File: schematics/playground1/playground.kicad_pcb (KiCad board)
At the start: 2 copper layers, 92.5 x 68.5 mm, 65 parts, among them J1 Conn_01x05, J2 Conn_02x03_Odd_Even, J3 Conn_01x03, J4 Conn_02x04_Odd_Even, SW1 SW_SPST, SW2 SW_Push, SW3 SW_Push, U1 ADS1299, U2 MCP1700x-330xxTT, U3 PIC32MX250F128B_I_SS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

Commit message: fixed all errors for pcb with no audio or ble
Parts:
- moved H1 0.50 mm to (96.0, 70.0)
- moved H2 0.50 mm to (180.5, 70.0)
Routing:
- net /AVDD_5V: track 90.4 -> 149.4 mm, vias 5 -> 8
- net /MCLR: track 45.2 -> 88.2 mm, vias 2 -> 8
- net /DGND: track 28.5 -> 67.7 mm, vias 5 -> 7
- net /DVDD_3V3: track 199.4 -> 232.0 mm, vias 4 -> 7
- net /RXD: track 46.9 -> 44.4 mm
- net /1P: track 20.4 -> 21.2 mm, vias 3 -> 2
- net /AGND: track 45.0 -> 45.3 mm, vias 13 -> 14
- net /BOOT_EN: vias 2 -> 4
- net /MOSI: vias 3 -> 2

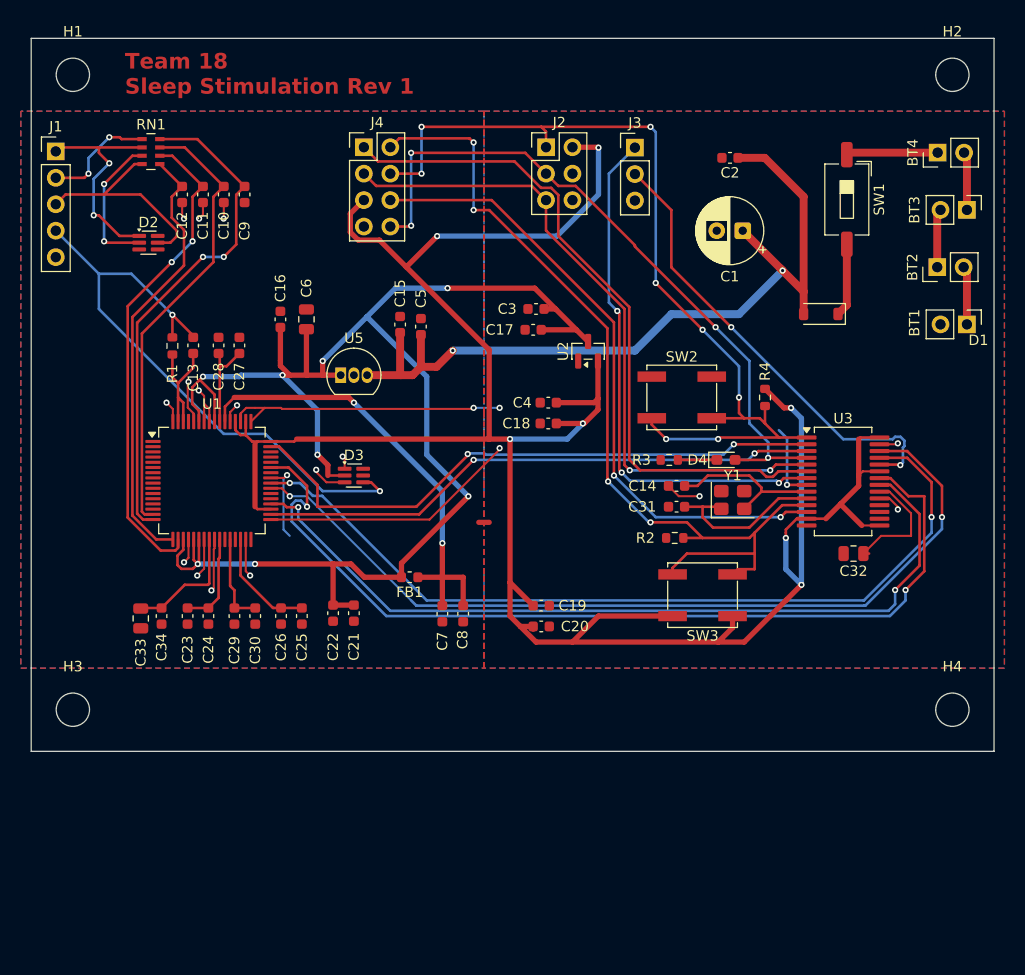
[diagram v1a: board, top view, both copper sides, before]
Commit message: add bluetooth chip to schematic and pcb
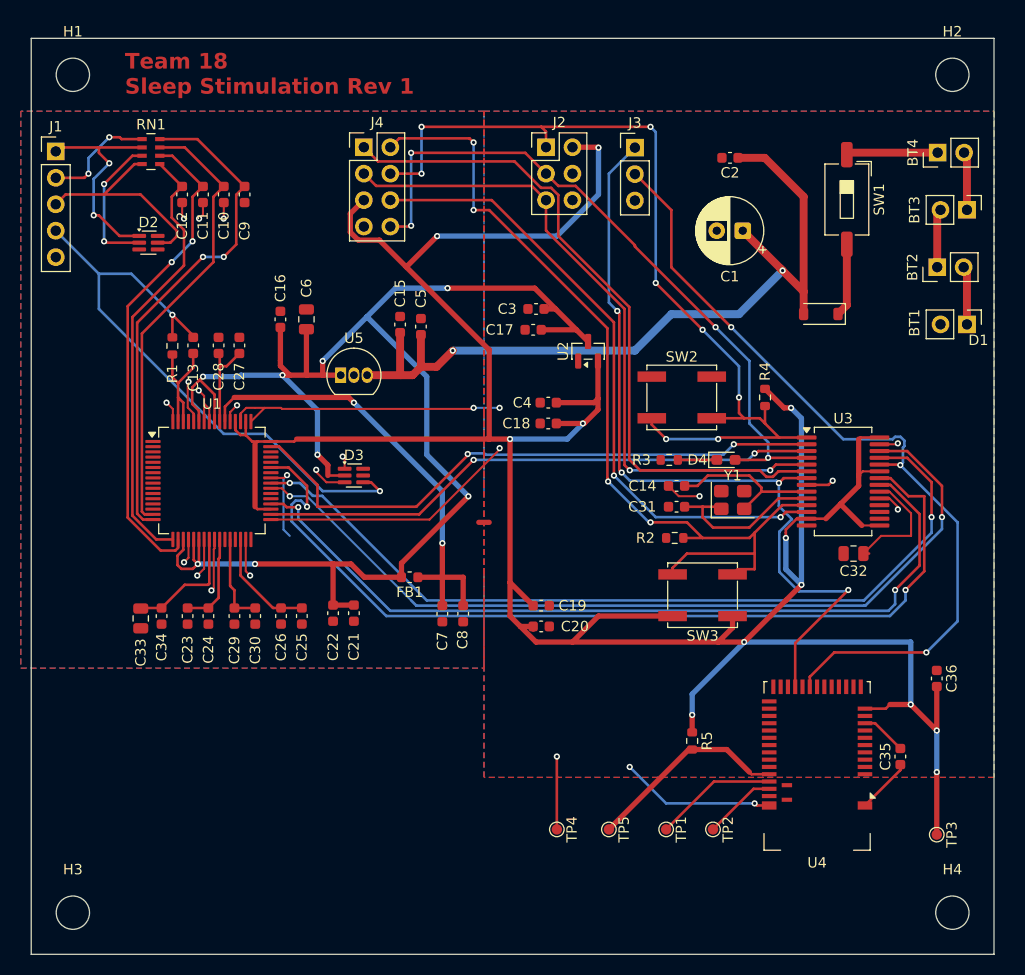
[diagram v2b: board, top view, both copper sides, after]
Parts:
- added C35: 1 µF, Capacitor_SMD:C_0603_1608Metric, F.Cu at (175.5, 135.5)
- added C36: 0.1 µF, Capacitor_SMD:C_0603_1608Metric, F.Cu at (179.0, 128.0)
- added R5: 10k, Resistor_SMD:R_0603_1608Metric, F.Cu at (155.5, 134.0)
- added TP1: TestPoint, TestPoint:TestPoint_Pad_D1.0mm, F.Cu at (153.0, 142.5)
- added TP2: TestPoint, TestPoint:TestPoint_Pad_D1.0mm, F.Cu at (157.5, 142.5)
- added TP3: TestPoint, TestPoint:TestPoint_Pad_D1.0mm, F.Cu at (179.0, 143.0)
- added TP4: TestPoint, TestPoint:TestPoint_Pad_D1.0mm, F.Cu at (142.5, 142.5)
- added TP5: TestPoint, TestPoint:TestPoint_Pad_D1.0mm, F.Cu at (147.5, 142.5)
- added U4: MDBT42Q-512K, ble_footprints:Raytac_MDBT42Q, F.Cu at (167.5, 136.4)
- moved H3 19.5 mm to (96.0, 150.5)
- moved H4 19.5 mm to (180.5, 150.5)
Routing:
- net /DVDD_3V3: track 232.0 -> 287.0 mm, vias 7 -> 12
- net /RXD: track 44.4 -> 79.1 mm, vias 2 -> 3
- net /TXD: track 51.1 -> 79.6 mm, vias 3 -> 4
- net /DGND: track 67.7 -> 90.2 mm, vias 7 -> 10
- net Net-(U4-P0.21/~{RESET}): track 0.00 -> 19.6 mm
- net Net-(U4-SWDCLK): track 0.00 -> 11.8 mm
- net Net-(U4-SWDIO): track 0.00 -> 7.02 mm
- net Net-(U4-DEC4): track 0.00 -> 4.40 mm
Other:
- board size 92.5 x 68.5 mm -> 92.5 x 88 mm

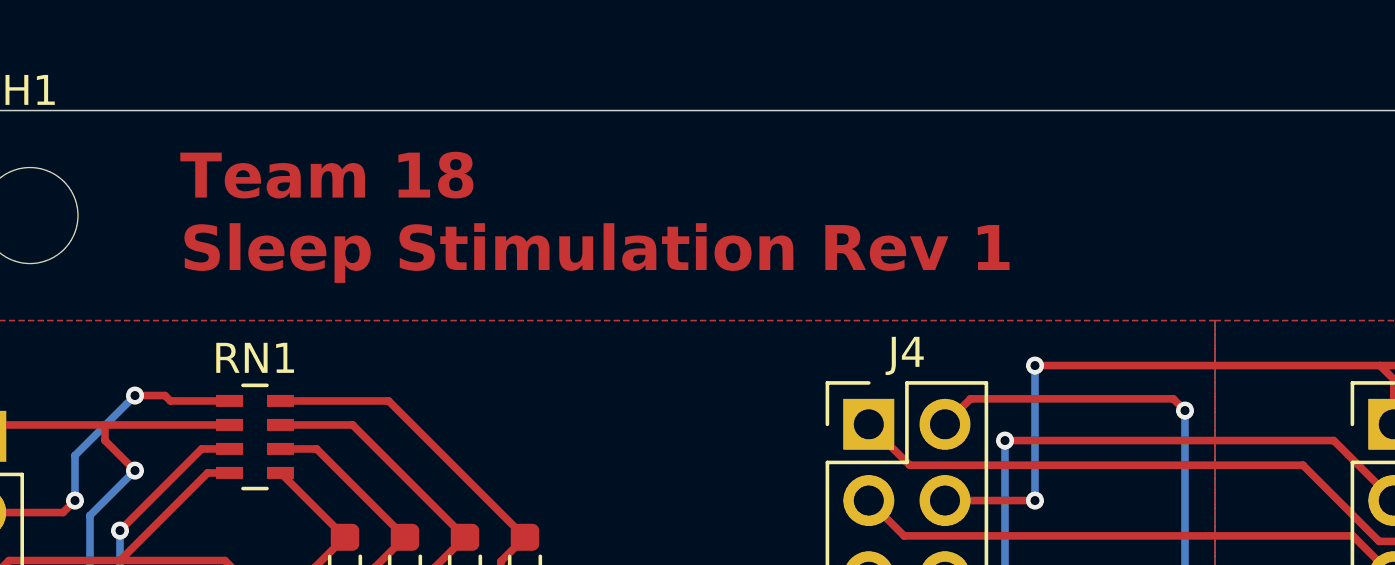
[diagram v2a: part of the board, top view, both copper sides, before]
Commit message: updated revision number for pcb
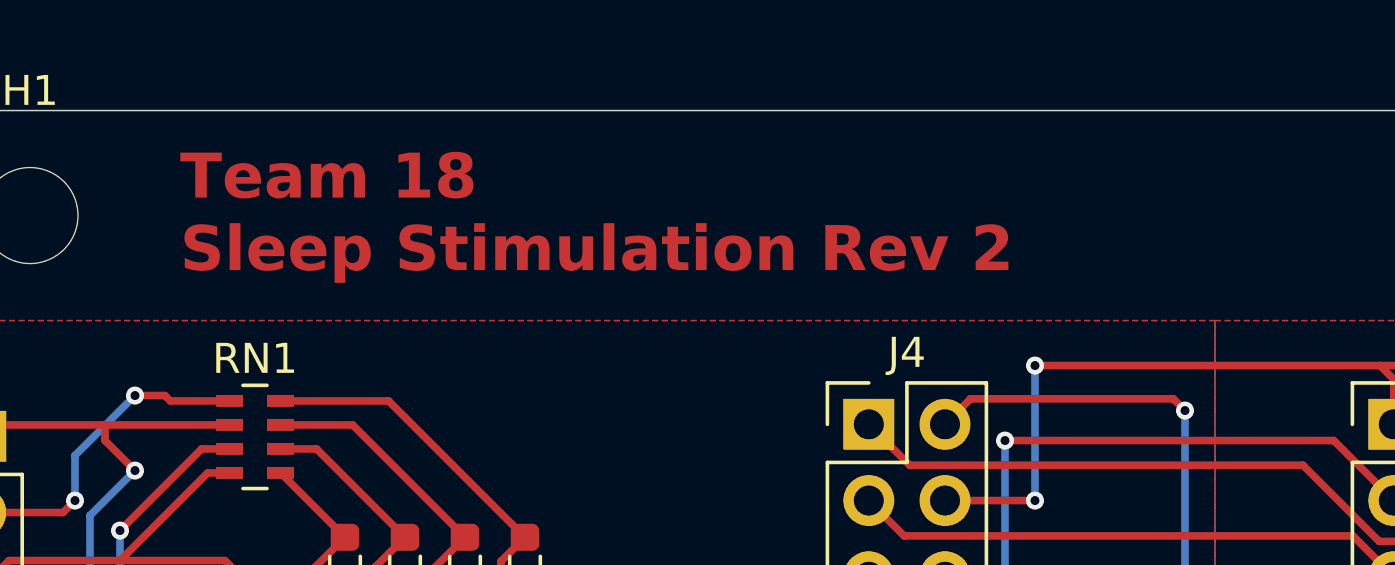
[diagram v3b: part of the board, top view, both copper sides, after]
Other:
- board text added: "Team 18 Sleep Stimulation Rev 2"
- board text removed: "Team 18 Sleep Stimulation Rev 1"
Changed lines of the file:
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@@
 		(layer "Edge.Cuts")
 	)
-	(gr_text "Team 18\nSleep Stimulation Rev 1"
+	(gr_text "Team 18\nSleep Stimulation Rev 2"
 		(at 101 72 0)
 		(layer "F.Cu")

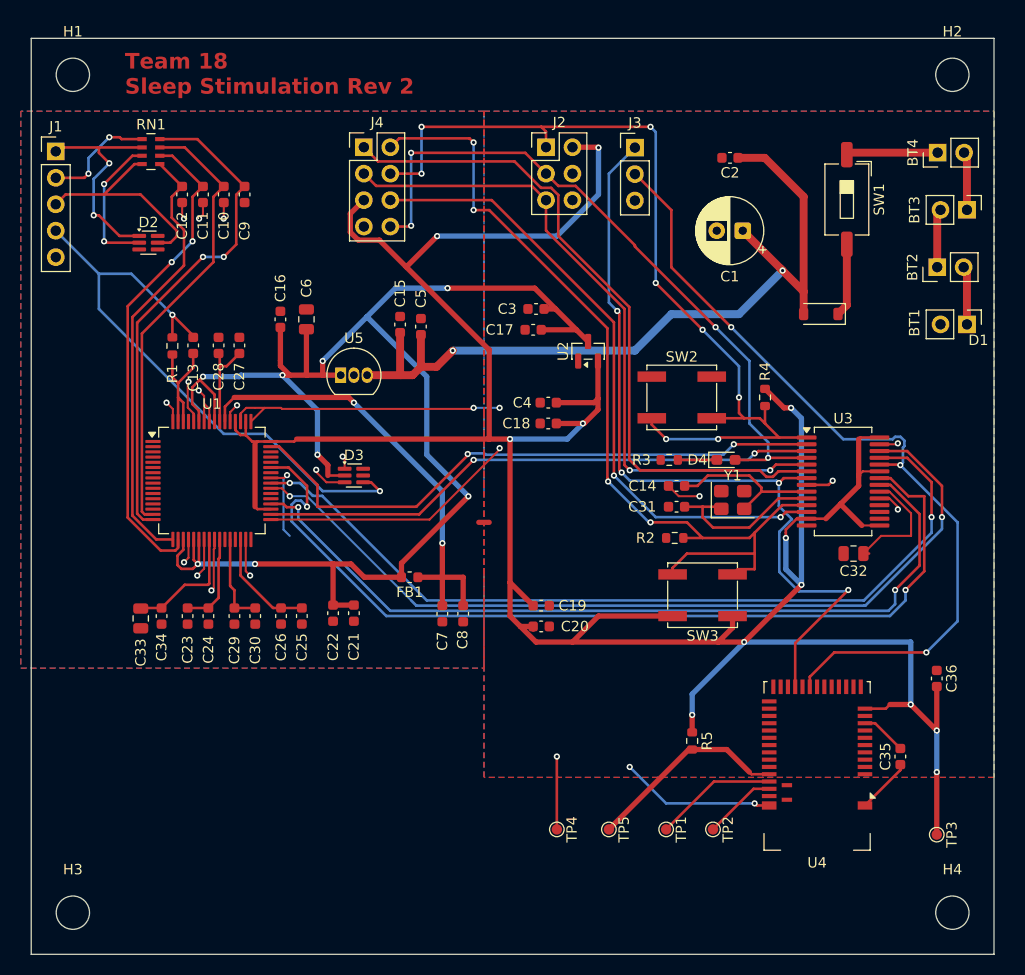
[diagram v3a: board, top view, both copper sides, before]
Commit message: clean up audio schematic, wire audio in and move ble
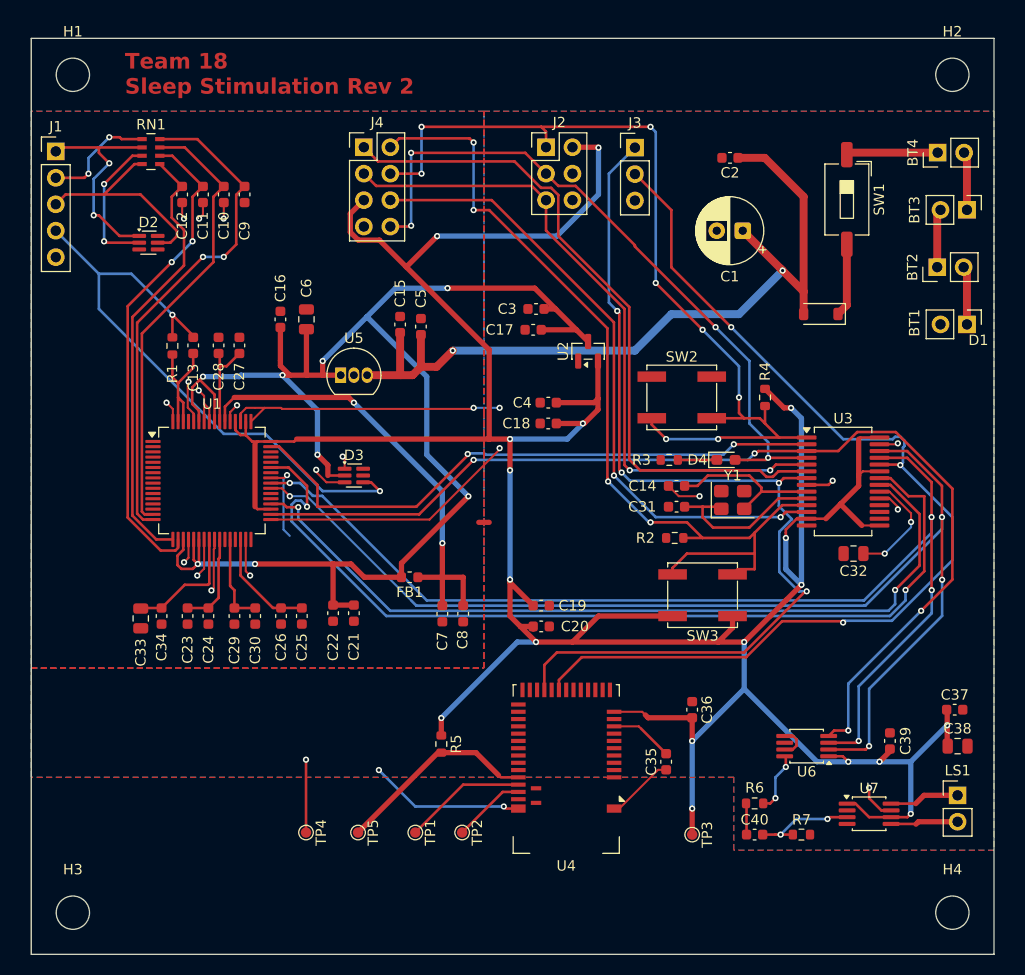
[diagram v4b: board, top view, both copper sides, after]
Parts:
- added C37: 0.1uF, Capacitor_SMD:C_0603_1608Metric, F.Cu at (180.7, 131.0)
- added C38: 10uF, Capacitor_SMD:C_0805_2012Metric, F.Cu at (181.0, 134.5)
- added C39: 0.1uF, Capacitor_SMD:C_0603_1608Metric, F.Cu at (174.5, 134.0)
- added C40: 1uF, Capacitor_SMD:C_0603_1608Metric, F.Cu at (161.5, 143.0)
- added LS1: Speaker, Connector_PinHeader_2.54mm:PinHeader_1x02_P2.54mm_Vertical, F.Cu at (181.0, 139.2)
- added R6: 1k, Resistor_SMD:R_0603_1608Metric, F.Cu at (161.5, 140.0)
- added R7: 100k, Resistor_SMD:R_0603_1608Metric, F.Cu at (166.0, 143.0)
- added U6: MCP4822, Package_SO:MSOP-8_3x3mm_P0.65mm, F.Cu at (166.5, 134.5)
- added U7: PAM8302AAS, Package_SO:MSOP-8_3x3mm_P0.65mm, F.Cu at (172.5, 141.0)
- moved R5 24.1 mm to (131.4, 134.3)
- moved TP1 24.1 mm to (128.9, 142.8)
- moved TP2 24.1 mm to (133.4, 142.8)
- moved TP4 24.1 mm to (118.4, 142.8)
- moved TP5 24.1 mm to (123.4, 142.8)
- moved U4 24.1 mm to (143.4, 136.7)
- moved C36 23.7 mm to (155.5, 131.0)
- moved TP3 23.5 mm to (155.5, 143.0)
- moved C35 22.5 mm to (153.0, 136.0)
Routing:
- net /MOSI: track 54.2 -> 100.7 mm, vias 2 -> 4
- net /DVDD_3V3: track 287.0 -> 319.0 mm, vias 12 -> 18
- net /CS1: track 83.7 -> 112.7 mm, vias 2 -> 4
- net /SCLK: track 81.7 -> 109.0 mm, vias 2 -> 4
- net /RXD: track 79.1 -> 99.3 mm
- net /TXD: track 79.6 -> 94.6 mm
- net Net-(U7-IN+): track 0.00 -> 9.98 mm, vias 0 -> 2
- net /DGND: track 90.2 -> 97.9 mm, vias 10 -> 11
- net Net-(U7-OUT-): track 0.00 -> 6.72 mm
- net Net-(U7-OUT+): track 0.00 -> 6.50 mm
- net Net-(U6-VA): track 0.00 -> 5.87 mm, vias 0 -> 2
- net Net-(C40-Pad1): track 0.00 -> 3.02 mm
- net Net-(U4-DEC4): track 4.40 -> 6.09 mm
- net Net-(U3-VCAP): track 11.9 -> 10.9 mm, vias 0 -> 2
- net Net-(U4-P0.21/~{RESET}): track 19.6 -> 19.0 mm

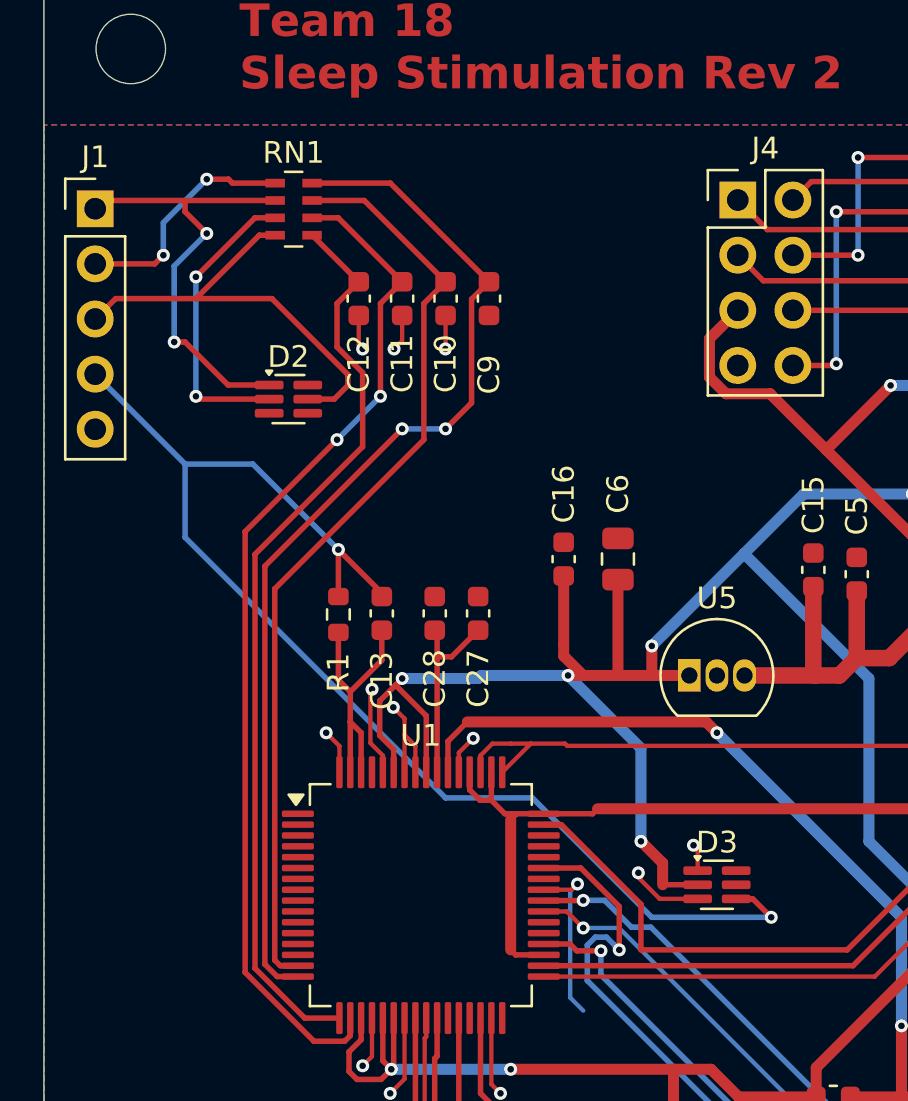
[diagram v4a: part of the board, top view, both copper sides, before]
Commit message: add tracing for new resistor / diode arrays
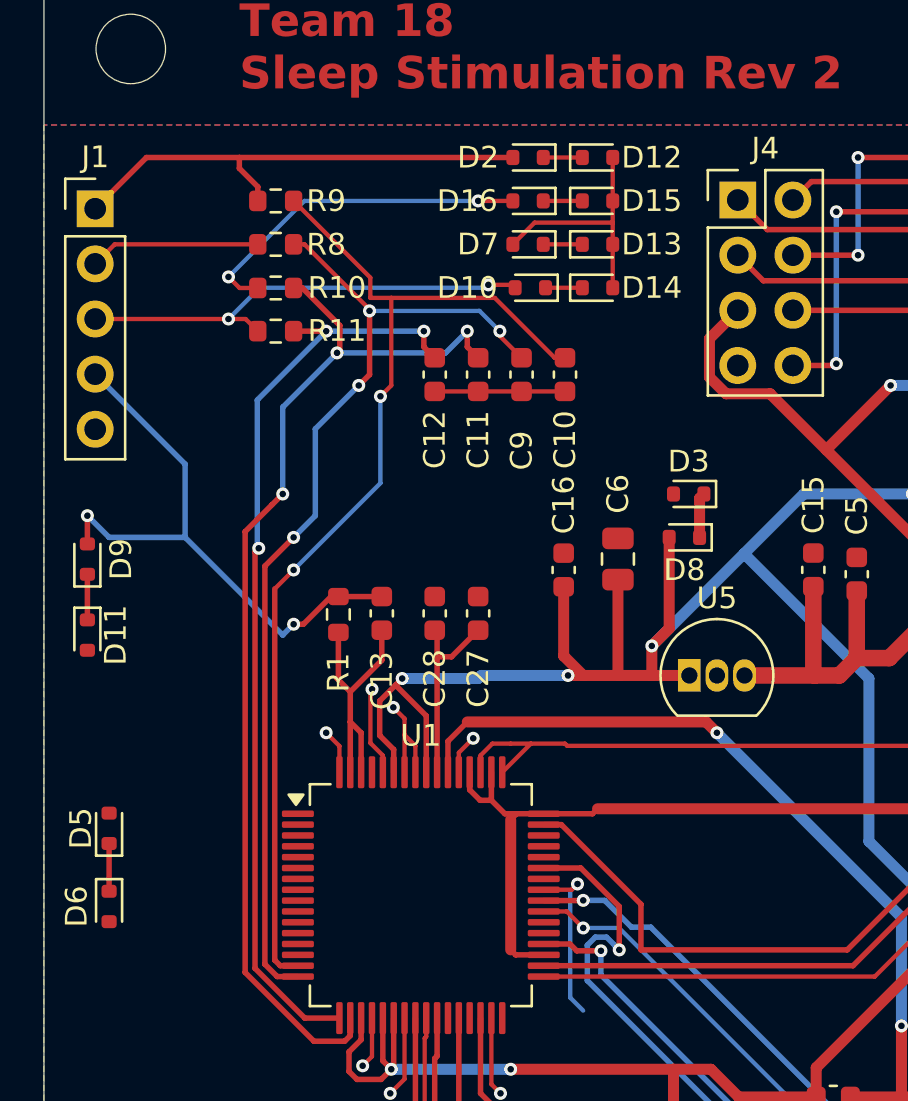
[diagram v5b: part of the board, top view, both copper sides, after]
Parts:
- removed RN1: 2.2k, Resistor_SMD:R_Array_Concave_4x0603
- added D10: 1N4148WT, Diode_SMD:D_SOD-523, F.Cu at (114.4, 81.0)
- added D11: 1N4148WT, Diode_SMD:D_SOD-523, F.Cu at (94.0, 97.0)
- added D12: 1N4148WT, Diode_SMD:D_SOD-523, F.Cu at (117.5, 75.0)
- added D13: 1N4148WT, Diode_SMD:D_SOD-523, F.Cu at (117.5, 79.0)
- added D14: 1N4148WT, Diode_SMD:D_SOD-523, F.Cu at (117.5, 81.0)
- added D15: 1N4148WT, Diode_SMD:D_SOD-523, F.Cu at (117.5, 77.0)
- added D16: 1N4148WT, Diode_SMD:D_SOD-523, F.Cu at (114.3, 77.0)
- added D5: 1N4148WT, Diode_SMD:D_SOD-523, F.Cu at (95.0, 105.9)
- added D6: 1N4148WT, Diode_SMD:D_SOD-523, F.Cu at (95.0, 109.5)
- added D7: 1N4148WT, Diode_SMD:D_SOD-523, F.Cu at (114.3, 79.0)
- added D8: 1N4148WT, Diode_SMD:D_SOD-523, F.Cu at (121.5, 92.5)
- added D9: 1N4148WT, Diode_SMD:D_SOD-523, F.Cu at (94.0, 93.5)
- added R10: 2.2K, Resistor_SMD:R_0603_1608Metric, F.Cu at (102.7, 81.0)
- added R11: 2.2K, Resistor_SMD:R_0603_1608Metric, F.Cu at (102.7, 83.0)
- added R8: 2.2K, Resistor_SMD:R_0603_1608Metric, F.Cu at (102.7, 79.0)
- added R9: 2.2K, Resistor_SMD:R_0603_1608Metric, F.Cu at (102.7, 77.0)
- D2, D3: value TPD4E1B06DCKR -> 1N4148WT; footprint Package_TO_SOT_SMD:SOT-363_SC-70-6 -> Diode_SMD:D_SOD-523
- moved D3 18.0 mm to (121.7, 90.5), turned to 180 degrees
- moved D2 15.7 mm to (114.3, 75.0), turned to 180 degrees
- moved C10 6.52 mm to (116.0, 85.0)
- moved C11 4.95 mm to (112.0, 85.0)
- moved C12 4.95 mm to (110.0, 85.0)
- moved C9 3.81 mm to (114.0, 85.0)
- moved C16 0.50 mm to (115.9, 94.0)
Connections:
- D2 pad 1: /1P -> Net-(D12-K)
- D2 pad 2: /SRB2 -> /1P
- D3 pad 1: /AGND -> Net-(D3-K)
- D3 pad 2: /AVDD_5V -> /AGND
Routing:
- net /BIAS: track 59.3 -> 27.3 mm
- net /AVDD_5V: track 149.4 -> 141.2 mm, vias 8 -> 7
- net /AGND: track 45.3 -> 52.8 mm, vias 14 -> 9
- net /IN1P: track 43.4 -> 49.9 mm, vias 0 -> 2
- net /1N: track 10.9 -> 7.86 mm, vias 2 -> 0
- net /SRB2: track 13.7 -> 16.1 mm
- net Net-(D5-K): track 0.00 -> 2.20 mm
- net /_SRB2: track 47.3 -> 49.4 mm, vias 2 -> 3
- net Net-(D11-K): track 0.00 -> 2.10 mm
- net Net-(D3-K): track 0.00 -> 2.08 mm
- net /IN1N: track 48.7 -> 46.8 mm, vias 2 -> 4
- net Net-(D15-K): track 0.00 -> 1.80 mm
- net Net-(D13-K): track 0.00 -> 1.80 mm
- net Net-(D12-K): track 0.00 -> 1.80 mm
- net Net-(D10-K): track 0.00 -> 1.69 mm
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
